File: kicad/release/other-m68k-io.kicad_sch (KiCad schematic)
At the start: 23 parts, among them J2 FTDI (GND CTS VCC TXD RXD RTS), J8 Expansion, SW1 RESET, U10 MC68681P, U13 MCP130T-450I/TT, Y1 3.6864MHz

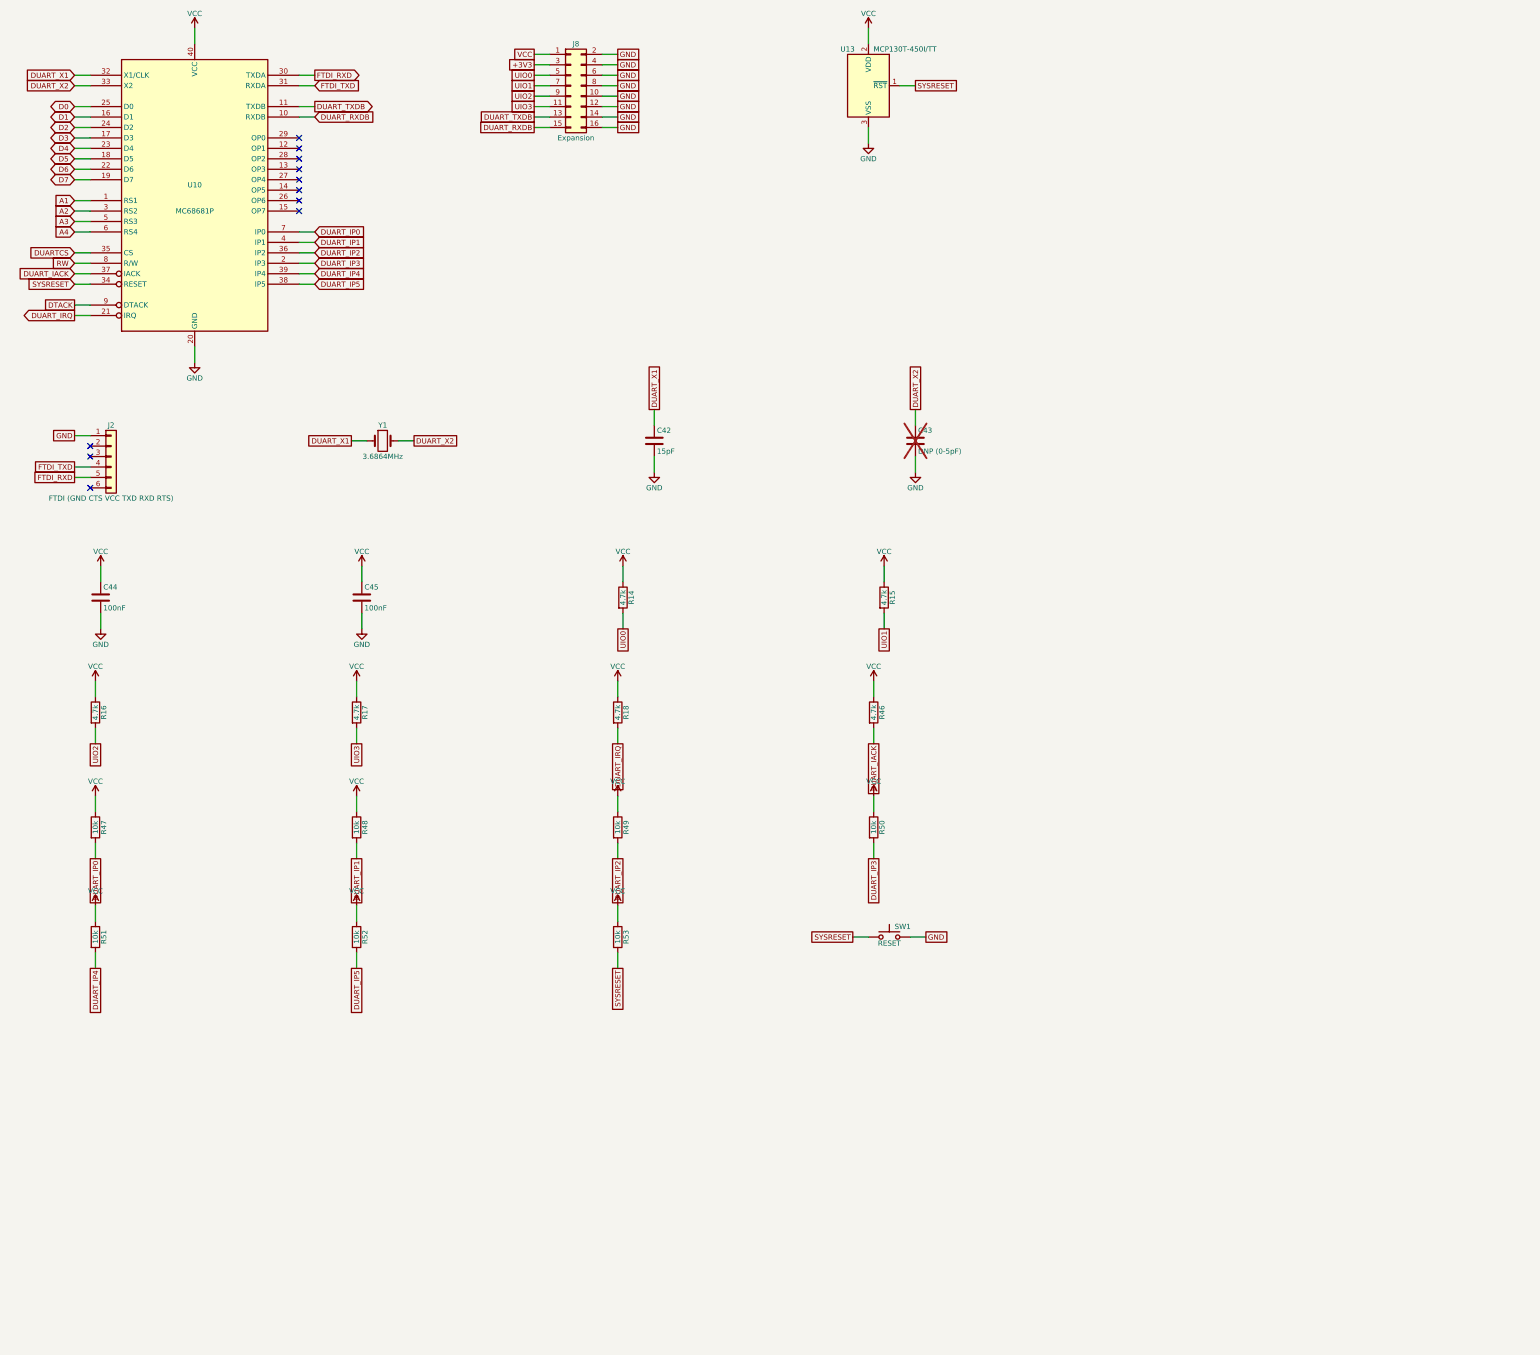
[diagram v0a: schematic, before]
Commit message: KiCad rev C1: native 4-bit SD bus (CLK, CMD, DAT0..3 straight from CPLD2 with 10 k pull-ups to 3.3 V, the three 1.8k/3.3k dividers removed, DAT1/DAT2 on CPLD2 pins 16/58), UIO0..3 removed from J8 (pins 5/7/9/11 n/c); ERC 0, DRC 0, rerouted (22 passes, 0 unrouted, 5146 segments, 530 vias); fab package and release snapshot regenerated; ORDER.md notes rev C1 vs the ordered B4
Co-Authored-By: Claude Fable 5.1 <noreply@anthropic.com>
Claude-Session: https://claude.ai/code/session_019bbFLKMxhKXGW6aABP44Z1
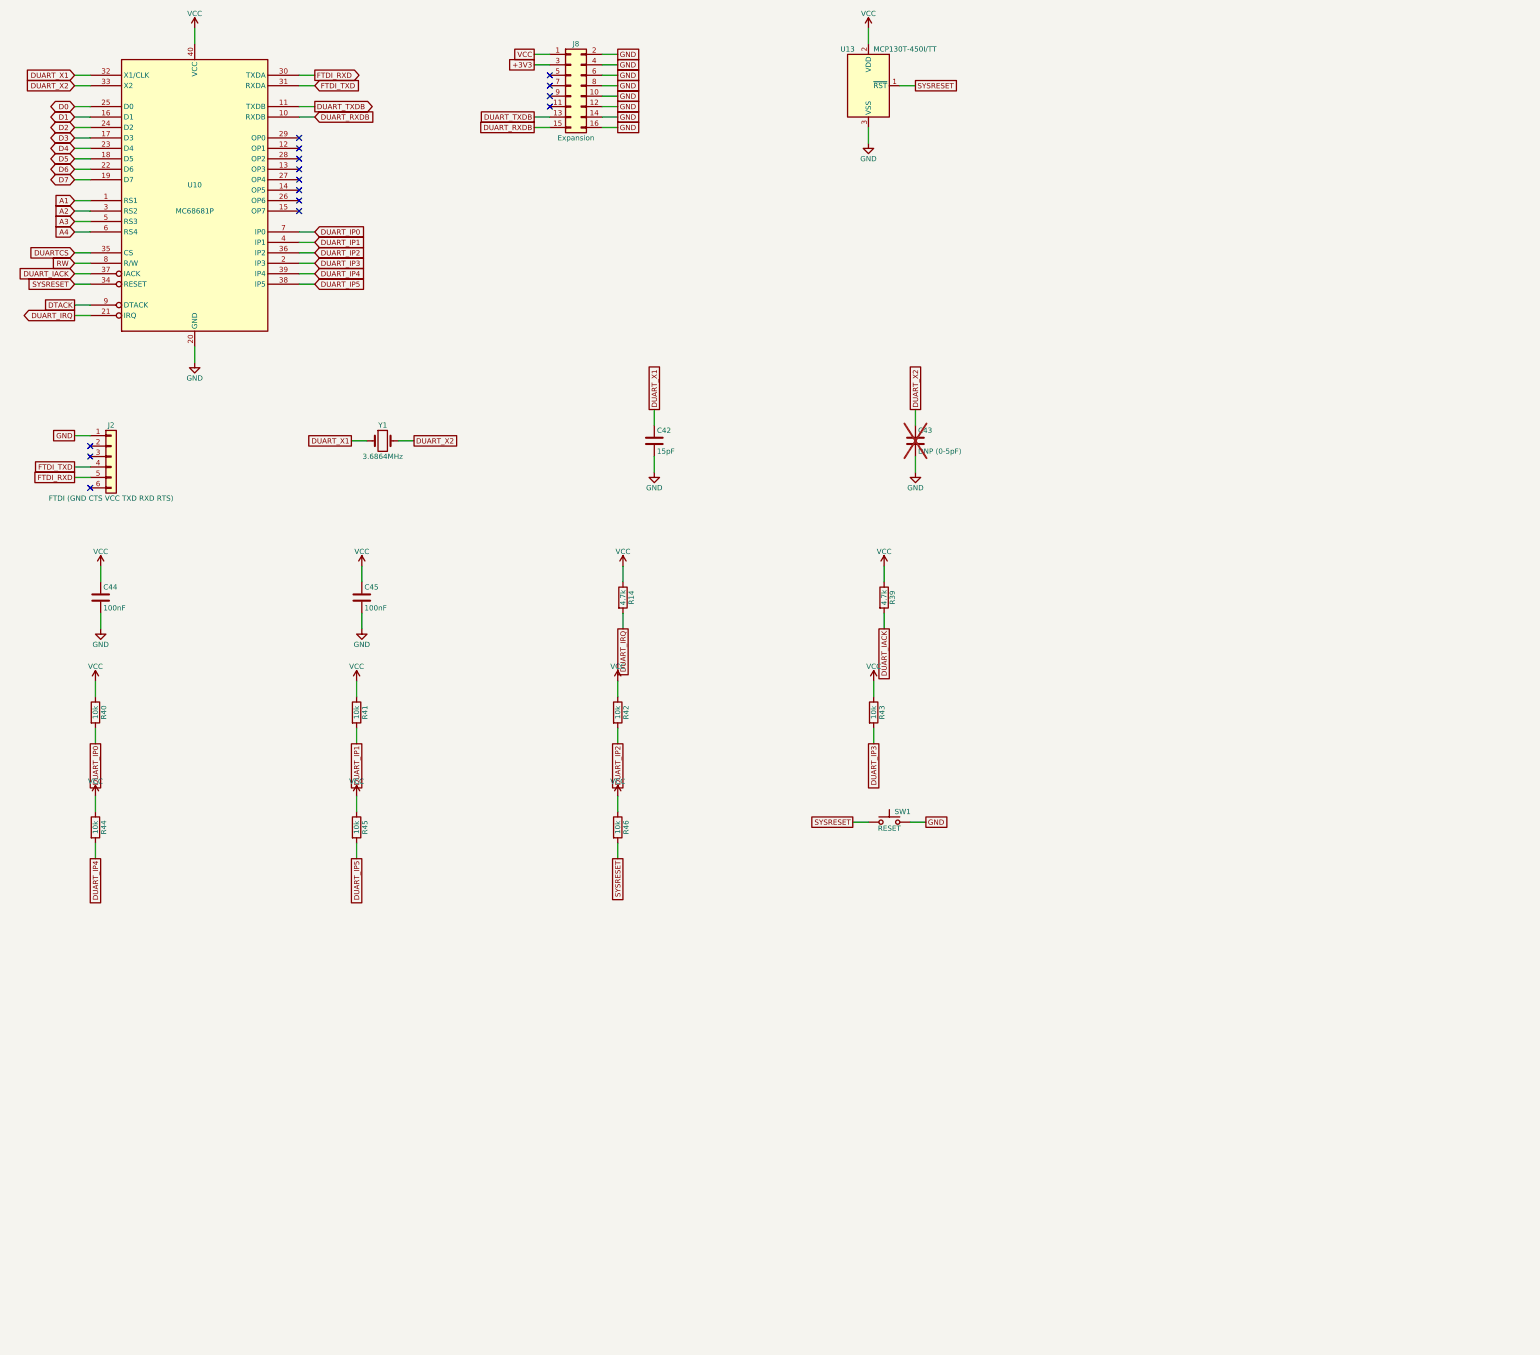
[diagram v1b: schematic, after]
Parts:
- removed R15, R16, R17, R18: 4.7k, Resistor_SMD:R_0603_1608Metric, symbol Device:R
- removed R47, R48, R49, R50, R51, R52, R53: 10k, Resistor_SMD:R_0603_1608Metric, symbol Device:R
- added R39: 4.7k, Resistor_SMD:R_0603_1608Metric, symbol Device:R
- added R40, R41, R42, R43, R44, R45: 10k, Resistor_SMD:R_0603_1608Metric, symbol Device:R
- R14: PcbNear J8 -> U10
- R46: value 4.7k -> 10k; Desc 4.7 k 1% 0603 -> 10 k 1% 0603; LCSC C23162 -> C25804; MPN RC0603FR-074K7L -> RC0603FR-0710KL; PcbNear U10 -> U13
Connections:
- net DUART_IACK: now also R39.2; no longer R46.2
- net DUART_IP0: now also R40.2
- net DUART_IP1: now also R41.2
- net DUART_IP2: now also R42.2
- net DUART_IP3: now also R43.2
- net DUART_IP4: now also R44.2
- net DUART_IP5: now also R45.2
- net DUART_IRQ: now also R14.2
- net SYSRESET: now also R46.2
- net VCC: now also R39.1, R40.1, R41.1, R42.1, R43.1, R44.1, R45.1
- net UIO0: no longer names the net of J8.5 (Pin_5)
- net UIO0: no longer R14.2
- net UIO1: no longer names the net of J8.7 (Pin_7)
- net UIO2: no longer names the net of J8.9 (Pin_9)
- net UIO3: no longer names the net of J8.11 (Pin_11)
- no-connect marks 11 -> 15
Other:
- moved on the sheet: R46, SW1
